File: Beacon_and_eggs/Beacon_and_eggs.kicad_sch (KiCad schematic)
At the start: 40 parts, among them J1 USB_C_Receptacle_USB2.0_16P, Q1 IRLML0030, SW1 Boot, SW2 Reset, U1 SA818V, U2 STM32F411CEUx, U3 ADXL343, U6 MCP1253-33X50I/MS, U7 MCP1253-33X50I/MS, Y1 25MHz 18pF, Y2 32.768kHz 12.5pF

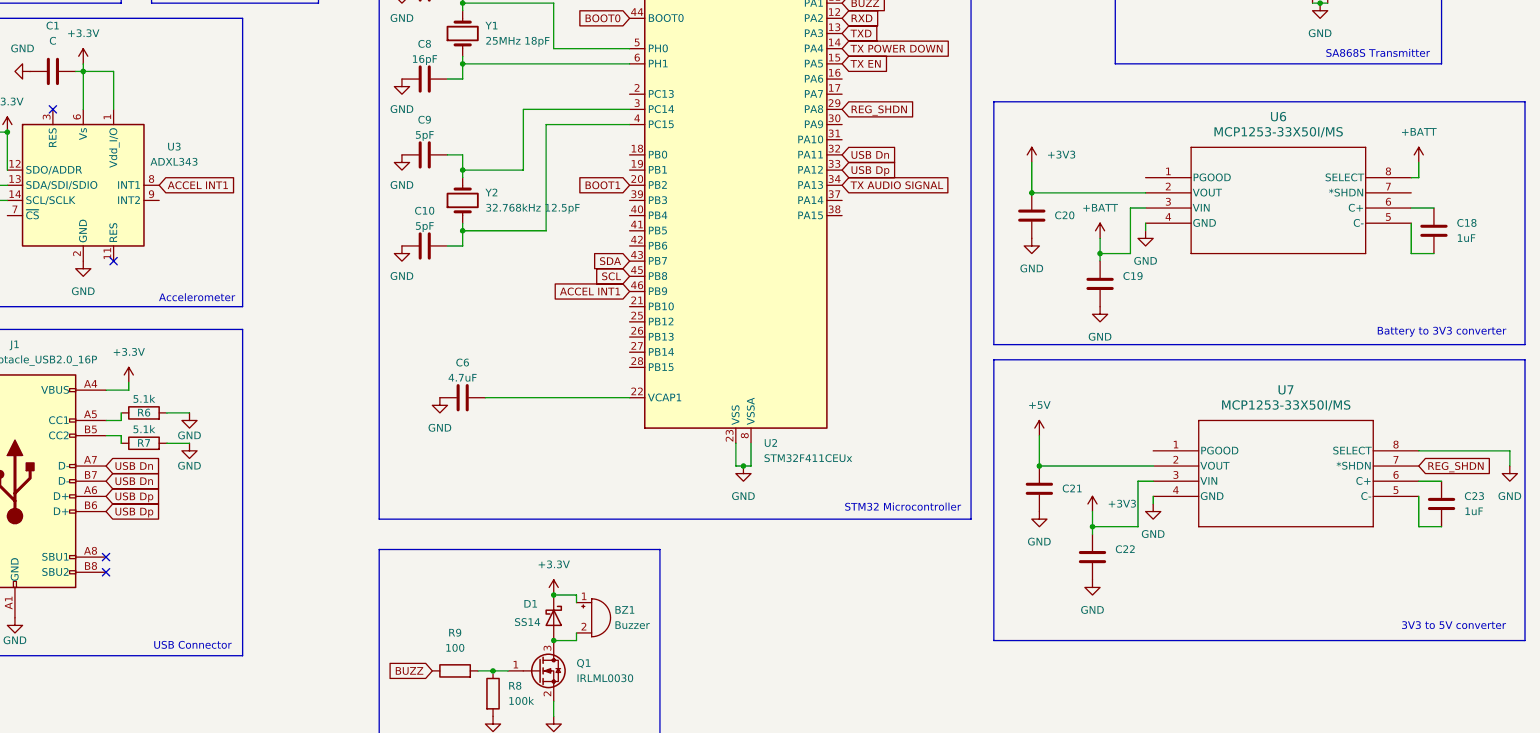
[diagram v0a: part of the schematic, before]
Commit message: Laid traces and changed 3.3V regulator
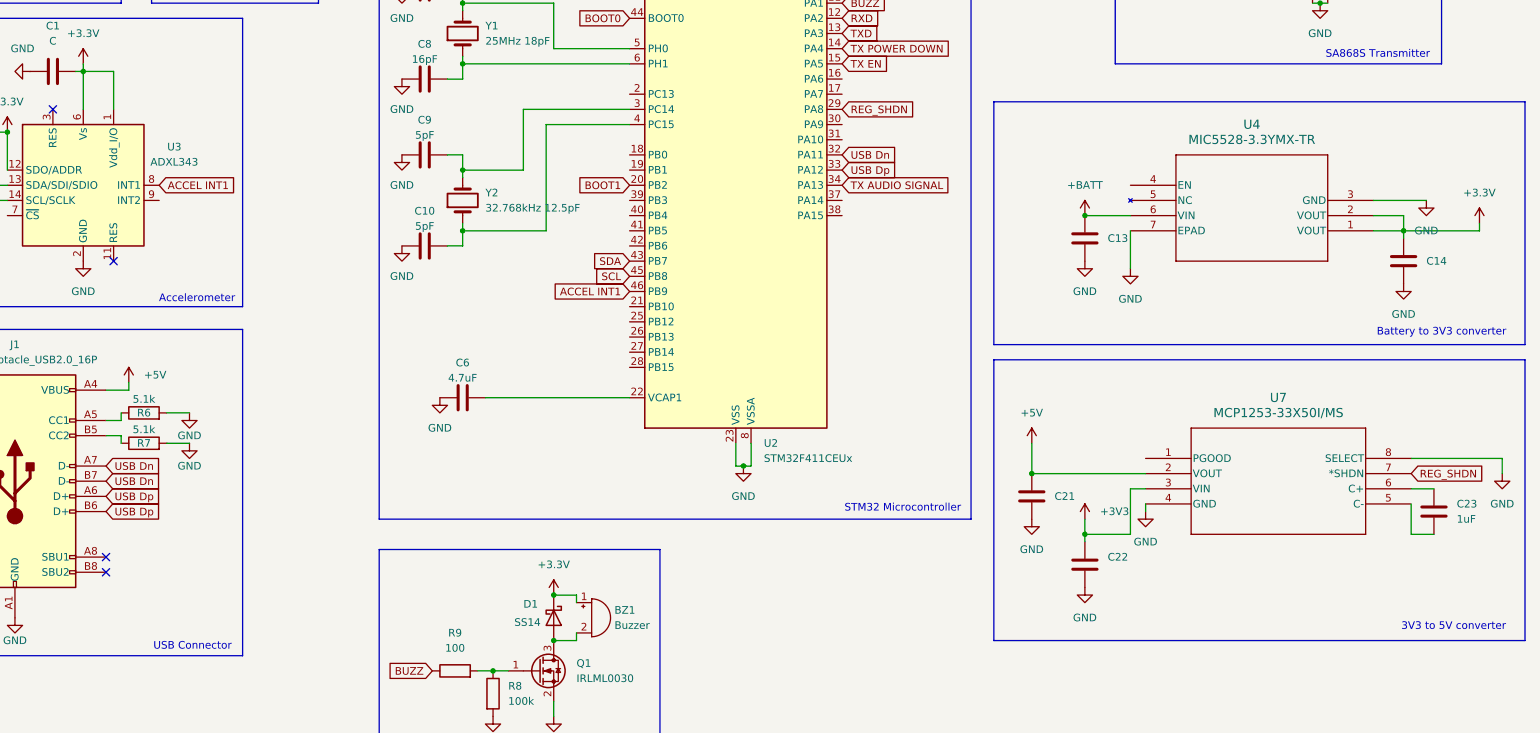
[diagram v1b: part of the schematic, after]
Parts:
- removed C18: 1uF, Capacitor_SMD:C_0603_1608Metric, symbol Device:C
- removed C19: 10uF, Capacitor_SMD:C_0603_1608Metric, symbol Device:C
- removed U6: MCP1253-33X50I/MS, Package_DFN_QFN:TDFN-8-1EP_3x2mm_P0.5mm_EP1.3x1.4mm, symbol 2025_26-UVR-Beacon:MCP1253-33X50I_MS
- added C14: 2.2uF, Capacitor_SMD:C_0603_1608Metric, symbol Device:C
- added U4: MIC5528-3.3YMX-TR, XTDFN6_1P2X1P2_MCH, symbol 2026-01-16_07-07-07:MIC5528-3.3YMX-TR
- C13: renamed from C20; value 10uF -> 2.2uF
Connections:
- net +3.3V: now also C14.1, U4.1 (VOUT), U4.2 (VOUT); no longer J1.A4 (VBUS), J1.A9 (VBUS), J1.B4 (VBUS), J1.B9 (VBUS)
- net +3V3: no longer C13.1
- net +5V: now also J1.A4 (VBUS), J1.A9 (VBUS), J1.B4 (VBUS), J1.B9 (VBUS)
- net +BATT: now also C13.1, U4.6 (VIN)
- net GND: now also C14.2, U4.3 (GND), U4.7 (EPAD)
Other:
- moved on the sheet: C13, C21, C22, C23, U7

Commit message: cheanged schematic and V1 pcb layout completed.
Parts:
- removed BZ1: Buzzer, symbol Device:Buzzer
- removed D1: SS14, Diode_SMD:D_SMA, symbol Diode:SS14
- removed Q1: IRLML0030, Package_TO_SOT_SMD:SOT-23, symbol Transistor_FET:IRLML0030
- removed SW1: Boot, symbol Switch:SW_MEC_5E
- removed SW2: Reset, symbol Switch:SW_MEC_5E
- removed U7: MCP1253-33X50I/MS, Package_DFN_QFN:TDFN-8-1EP_3x2mm_P0.5mm_EP1.3x1.4mm, symbol 2025_26-UVR-Beacon:MCP1253-33X50I_MS
- added 3V3: 3V3, TestPoint:TestPoint_THTPad_D1.5mm_Drill0.7mm, symbol Connector:TestPoint
- added C15: 10uF, Capacitor_SMD:C_0402_1005Metric_Pad0.74x0.62mm_HandSolder, symbol Device:C
- added C16, C18, C20: 0.1uF, Capacitor_SMD:C_0402_1005Metric_Pad0.74x0.62mm_HandSolder, symbol Device:C
- added C17: 1nF, Capacitor_SMD:C_0402_1005Metric_Pad0.74x0.62mm_HandSolder, symbol Device:C_Small
- added C19: 33uF, Capacitor_SMD:C_0402_1005Metric_Pad0.74x0.62mm_HandSolder, symbol Device:C
- added C24: 10nF, Capacitor_SMD:C_0402_1005Metric_Pad0.74x0.62mm_HandSolder, symbol Device:C
- added C25: 33nF, Capacitor_SMD:C_0402_1005Metric_Pad0.74x0.62mm_HandSolder, symbol Device:C
- added D1, D3: UCLAMP3311P.TCT, Diode_SMD:D_0402_1005Metric_Pad0.77x0.64mm_HandSolder, symbol APV2:UCLAMP3311P.TCT
- added D2: RED LED, LED_SMD:LED_0402_1005Metric_Pad0.77x0.64mm_HandSolder, symbol Device:LED
- added D4: BLUE LED, LED_SMD:LED_0402_1005Metric_Pad0.77x0.64mm_HandSolder, symbol Device:LED
- added D5: GREEN LED, LED_SMD:LED_0402_1005Metric_Pad0.77x0.64mm_HandSolder, symbol Device:LED
- added J2: Conn_01x03_Pin, Connector_PinHeader_2.54mm:PinHeader_1x03_P2.54mm_Vertical, symbol Connector:Conn_01x03_Pin
- added J3: Conn_01x02_Pin, Connector_JST:JST_PH_B2B-PH-K_1x02_P2.00mm_Vertical, symbol Connector:Conn_01x02_Pin
- added Q1: NTA4151P, NTA4151PT1G:SOT50P160X90-3N, symbol APV2:NTA4151P
- added Q2: NTA4153N, NTA4151PT1G:SOT50P160X90-3N, symbol APV2:NTA4153N
- added R10, R11, R18: 51k, Resistor_SMD:R_0402_1005Metric_Pad0.72x0.64mm_HandSolder, symbol Device:R
- added R12: 250R, Resistor_SMD:R_0402_1005Metric_Pad0.72x0.64mm_HandSolder, symbol Device:R
- added R13: 37.4K, Resistor_SMD:R_0402_1005Metric_Pad0.72x0.64mm_HandSolder, symbol Device:R
- added R14, R15: 1.5K, Resistor_SMD:R_0402_1005Metric_Pad0.72x0.64mm_HandSolder, symbol Device:R
- added R16: 510k, Resistor_SMD:R_0402_1005Metric_Pad0.72x0.64mm_HandSolder, symbol Device:R
- added R17: 50R, Resistor_SMD:R_0402_1005Metric_Pad0.72x0.64mm_HandSolder, symbol Device:R
- added R19: 3.3K, Resistor_SMD:R_0402_1005Metric_Pad0.72x0.64mm_HandSolder, symbol Device:R
- added R20: 1K, Resistor_SMD:R_0402_1005Metric_Pad0.72x0.64mm_HandSolder, symbol Device:R
- added SIG: FABRIC_ANT_HOLES, MountingHole:MountingHole_3.2mm_M3_DIN965_Pad_TopBottom, symbol Connector:Conn_01x02_Pin
- added SW3: RESET, Button_Switch_SMD:SW_SPST_PTS810, symbol Switch:SW_MEC_5G
- added SW4: BOOT0, Button_Switch_SMD:SW_SPST_PTS810, symbol Switch:SW_MEC_5G
- added TP3: SCL, TestPoint:TestPoint_THTPad_D1.5mm_Drill0.7mm, symbol Connector:TestPoint
- added TP4: SDA, TestPoint:TestPoint_THTPad_D1.5mm_Drill0.7mm, symbol Connector:TestPoint
- added TP5: VBAT, TestPoint:TestPoint_THTPad_D1.5mm_Drill0.7mm, symbol Connector:TestPoint
- added TP6: VSYS, TestPoint:TestPoint_THTPad_D1.5mm_Drill0.7mm, symbol Connector:TestPoint
- added U6: BQ24070RHLR, Package_SO:HTSSOP-20-1EP_4.4x6.5mm_P0.65mm_EP3.4x6.5mm_Mask2.4x3.7mm, symbol BQ24070RHLR:BQ24070RHLR
- C1: value C -> 0.1F; footprint Capacitor_SMD:C_0603_1608Metric -> Capacitor_SMD:C_0402_1005Metric_Pad0.74x0.62mm_HandSolder
- C10, C7, C8, C9: footprint Capacitor_SMD:C_0201_0603Metric -> Capacitor_SMD:C_0402_1005Metric_Pad0.74x0.62mm_HandSolder
- C11, C12, C13, C14, C21: footprint Capacitor_SMD:C_0603_1608Metric -> Capacitor_SMD:C_0402_1005Metric_Pad0.74x0.62mm_HandSolder
- C2, C3, C6: footprint Capacitor_SMD:C_0201_0603Metric -> Capacitor_SMD:C_0201_0603Metric_Pad0.64x0.40mm_HandSolder
- C22: value 10uF -> 0.1uF; footprint Capacitor_SMD:C_0603_1608Metric -> Capacitor_SMD:C_0402_1005Metric_Pad0.74x0.62mm_HandSolder
- C23: value 1uF -> 10uF; footprint Capacitor_SMD:C_0603_1608Metric -> Capacitor_SMD:C_0402_1005Metric_Pad0.74x0.62mm_HandSolder
- C4, C5: footprint Capacitor_SMD:C_0603_1608Metric -> Capacitor_SMD:C_0201_0603Metric_Pad0.64x0.40mm_HandSolder
- J1: footprint (none) -> Connector_USB:USB_C_Receptacle_GCT_USB4105-xx-A_16P_TopMnt_Horizontal
- R1, R2, R3, R4, R5, R6, R7: footprint Resistor_SMD:R_0603_1608Metric -> Resistor_SMD:R_0402_1005Metric_Pad0.72x0.64mm_HandSolder
- R8: value 100k -> 250R; footprint Resistor_SMD:R_0603_1608Metric -> Resistor_SMD:R_0402_1005Metric_Pad0.72x0.64mm_HandSolder
- R9: value 100 -> 250R; footprint Resistor_SMD:R_0603_1608Metric -> Resistor_SMD:R_0402_1005Metric_Pad0.72x0.64mm_HandSolder
- U4: footprint XTDFN6_1P2X1P2_MCH -> footprints:XTDFN6_1P2X1P2_MCH
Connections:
- net +3V3 is gone; now on net VBUS: C22.1
- net +BATT is gone; now on net VSYS: C13.1, U4.6 (VIN)
- net +3.3V: now also 3V3.1, R17.1, SW4.3 (B), SW4.4 (B); no longer C1.2, U1.8 (VDD), U3.1 (Vdd_I/O)
- net BOOT0: now also R1.2, SW4.1 (A), SW4.2 (A); no longer R1.1
- net GND: now also C1.2, C23.2, R1.1, C15.2, C16.2, C17.2, C18.2, C19.2, C20.2, C24.2, C25.2, D1.1 (A1), D3.1 (A1), D4.1 (K), J2.3 (Pin_3), J3.2 (Pin_2), Q2.2 (S), R13.2, R16.2, R18.1, R20.2, SIG.2 (Pin_2), SW3.3 (B), SW3.4 (B), U6.11 (VSS_11), U6.19 (GND_19), U6.20 (GND_20), U6.21 (VSS_21), U6.22 (VSS_21), U6.23 (VSS_21), U6.24 (VSS_21), U6.25 (VSS_21), U6.26 (VSS_21), U6.27 (VSS_21), U6.28 (VSS_21), U6.29 (VSS_21), U6.8 (MODE); no longer C1.1, R1.2, R8.2
- net NRST: now also SW3.1 (A), SW3.2 (A)
- net SCL: now also R4.1, TP3.1; no longer R5.1
- net SDA: now also R5.1, TP4.1; no longer R4.1
- net X2_OUT: now reaches C10.2, U2.4 (PC15), Y2.1
- net X2_IN: now reaches C9.2, U2.3 (PC14), Y2.2
- net VBUS: now reaches C23.1
- net VBUS: now also J1.A4 (VBUS), J1.A9 (VBUS), J1.B4 (VBUS), J1.B9 (VBUS), U6.4 (IN)
- net LED1: now reaches U2.17 (PA7)
- net LED1: now also R12.1
- net TX_AUDIO_SIGNAL: now reaches U2.31 (PA10)
- net TX_AUDIO_SIGNAL: now also R19.1
- net SWCLK: now reaches U2.37 (PA14)
- net SWCLK: now also R9.1, J2.1 (Pin_1)
- net BATT_V_ADC: now reaches U2.38 (PA15)
- net BATT_V_ADC: now also C17.1, R11.1, R18.2
- net BATT_EN: now reaches U2.41 (PB5)
- net BATT_EN: now also Q2.1 (G), R16.1
- net X1_IN: now reaches C7.2, U2.5 (PH0), Y1.2
- net X1_OUT: now reaches C8.2, U2.6 (PH1), Y1.1
- net at R9.2: now also D3.2 (A2); no longer R8.1
- net VSYS: now reaches U4.4 (EN)
- net VSYS: now also C21.1, U1.8 (VDD), C16.1, C20.1, TP6.1, U6.15 (OUT_15), U6.16 (OUT_16), U6.17 (OUT_17)
- removed net +5V: C21.1, J1.A4 (VBUS), J1.A9 (VBUS), J1.B4 (VBUS), J1.B9 (VBUS)
- net ACCEL INT1 renamed ACCEL_INT1
- net BUZZ: no longer names the net of U2.11 (PA1)
- net BUZZ: no longer R9.1
- net REG_SHDN: no longer names the net of U2.29 (PA8)
- net RF_IN renamed ANT_SIG
- net ANT_SIG: now also SIG.1 (Pin_1)
- net TX AUDIO SIGNAL: no longer names the net of U1.18 (MIC_IN)
- net TX AUDIO SIGNAL: now also C25.1, R19.2; no longer U2.34 (PA13)
- net TX EN renamed TX_EN
- net TX POWER DOWN renamed TX_PWR_DN
- net USB Dn renamed USB_DN
- net USB Dp renamed USB_DP
- new net: Q1.3 (D1), Q1.8 (D1), R11.2
- new net: R20.1, U6.10 (ISET1)
- new net: C24.1, R13.1, U6.13 (DPPM)
- new net: D2.1 (K), U6.2 (STAT1)
- new net: D5.1 (K), U6.3 (STAT2)
- new net: C15.1, R17.2
- new net: D4.2 (A), R12.2
- new net: C1.1, U3.1 (Vdd_I/O)
- new net: D5.2 (A), R14.2
- new net: D2.2 (A), R15.2
- new net: D1.2 (A2), R8.1
- new net: Q1.1 (G1), Q2.3 (D), R10.1
- new net SWDIO: J2.2 (Pin_2), R8.2, U2.34 (PA13)
- new net VBAT: C19.1, J3.1 (Pin_1), Q1.2 (S1), R10.2, TP5.1, U6.5 (BAT_5), U6.6 (BAT_6)
- new net VREF: C18.1, R14.1, R15.1, U6.1 (VREF), U6.14 (TMR), U6.7 (ISET2), U6.9 (CE)
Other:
- note added: "ACCEELEROMETER"
- note added: "ANTENNA INPUT"
- note added: "BATTERY CHARGER AND FLOW CONTROL"
- note added: "BATTERY CONNECTOR"
- note added: "BATTERY MONITORING CIRCUIT"
- note added: "BOOT CIRCUIT"
- note added: "MICROCONTROLLER"
- note added: "Pads are plated mounting holes used as RF feed and GND clamp for fabric antenna. No connector installed"
- note added: "RESET CIRCUIT"
- note added: "SA868S TRANSMITTER"
- note added: "SWD CONNECTOR"
- note added: "TEST POINTS"
- note added: "USB-C CONNECTOR"
- note added: "VSYS TO 3V3 REG"
- note removed: "3V3 to 5V converter"
- note removed: "Accelerometer"
- note removed: "Battery to 3V3 converter"
- note removed: "Boot circuit"
- note removed: "Buzzer"
- note removed: "Reset circuit"
- note removed: "SA868S Transmitter"
- note removed: "STM32 Microcontroller"
- note removed: "USB Connector"
- moved on the sheet: C10, C11, C12, C2, C3, C4, C5, C6, C7, C8, C9, J1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

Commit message: narrowed the pcb down from 60mm to 40 mm
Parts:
- renumbered SIG to SIG1
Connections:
- net ACCEL_INT1: now also U2.2 (PC13); no longer U2.46 (PB9)
- net BATT_EN: now also U2.28 (PB15); no longer U2.41 (PB5)
- net BATT_V_ADC: now also U2.16 (PA6); no longer U2.38 (PA15)
- net LED1: now also U2.13 (PA3); no longer U2.17 (PA7)
- net RXD: now also U2.18 (PB0); no longer U2.12 (PA2)
- net TXD: now also U2.25 (PB12); no longer U2.13 (PA3)
- net TX_AUDIO_SIGNAL: now also U2.26 (PB13); no longer U2.31 (PA10)
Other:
- moved on the sheet: C10, C7, C8, C9, Y1, Y2

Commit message: Added complete BOM, replaced a footprint, added missing STEP files
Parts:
- 3V3: Manufacturer (none) -> C0402C104K4RACTU; now left out of the parts list
- C1: value 0.1F -> 0.1uF; DigiKey_Part_Number (none) -> C0402C104K4RACTU
- C10, C9: DigiKey_Part_Number (none) -> GRM1555C1H5R0BA01D
- C11, C12: value 0.1uf -> 0.1uF; DigiKey_Part_Number (none) -> C0402C104K4RACTU
- C13, C14: DigiKey_Part_Number (none) -> GRM155C80J225KE95D
- C15, C21, C23: DigiKey_Part_Number (none) -> GRM155R61A106ME11D
- C16, C18, C20, C22: DigiKey_Part_Number (none) -> C0402C104K4RACTU
- C17: DigiKey_Part_Number (none) -> C0402C102K5RACTU; Manufacturer Part Number 0201B102K250CT -> (none)
- C19: footprint Capacitor_SMD:C_0402_1005Metric_Pad0.74x0.62mm_HandSolder -> Capacitor_SMD:C_0805_2012Metric; DigiKey_Part_Number (none) -> C2012X5R0J336M125AC
- C2, C3, C4, C5: DigiKey_Part_Number (none) -> GRM033C71C104KE14D
- C24: DigiKey_Part_Number (none) -> GRM155R71C103KA01D
- C25: DigiKey_Part_Number (none) -> C0402C333J4RACTU
- C6: DigiKey_Part_Number (none) -> GRM155R60J475ME87D
- C7, C8: DigiKey_Part_Number (none) -> GJM1555C1H160FB01J
- D1, D3: DigiKey_Part_Number (none) -> UCLAMP3311P.TCT
- D2: DigiKey_Part_Number (none) -> SML-D12U1WT86
- D4: footprint LED_SMD:LED_0402_1005Metric_Pad0.77x0.64mm_HandSolder -> LED_SMD:LED_0805_2012Metric; DigiKey_Part_Number (none) -> 150080BS75000; Manufacturer Part Number 150080BS75000 -> (none)
- D5: DigiKey_Part_Number (none) -> 150060GS75000
- J1: DigiKey_Part_Number (none) -> USB4215-03-A
- J2, J3, SIG1, TP3, TP4, TP5, TP6: now left out of the parts list
- Q1: DigiKey_Part_Number (none) -> NTA4151PT1G
- Q2: DigiKey_Part_Number (none) -> NTA4153NT1G
- R1, R2, R3: DigiKey_Part_Number (none) -> RMCF0402FT10K0
- R10, R11, R18: DigiKey_Part_Number (none) -> ERA-2AEB513X; Manufacturer Part Number RC0201FR-0751KL -> (none)
- R12: DigiKey_Part_Number (none) -> RE0402BRE07250RL; Manufacturer Part Number RMCF0603FT22R0 -> (none)
- R13: DigiKey_Part_Number (none) -> ERJ-2RKF3742X
- R14, R15: DigiKey_Part_Number (none) -> RC0402FR-071K5L
- R16: DigiKey_Part_Number (none) -> RC0402FR-07510KL; Manufacturer Part Number RC0201FR-07510KL -> (none)
- R17: DigiKey_Part_Number (none) -> RT0402BRE0750RL
- R19: DigiKey_Part_Number (none) -> ERA-2AEB332X
- R20: DigiKey_Part_Number (none) -> RC0402FR-071KL
- R4, R5: DigiKey_Part_Number (none) -> RC0402JR-074K7L
- R6, R7: DigiKey_Part_Number (none) -> RC0402FR-075K1L
- R8, R9: DigiKey_Part_Number (none) -> RE0402BRE07250RL
- SW3, SW4: DigiKey_Part_Number (none) -> PTS810SJK250SMTR LFS
- U1: value SA818V -> SA868S; DigiKey_Part_Number (none) -> SA868S
- U2: value STM32F411CEUx -> STM32F411CEU6TR; DigiKey_Part_Number (none) -> STM32F411CEU6TR
- U3: DigiKey_Part_Number (none) -> ADXL343BCCZ-RL7
- U4: DigiKey_Part_Number (none) -> MIC5528-3.3YMX-TR
- U6: footprint Package_SO:HTSSOP-20-1EP_4.4x6.5mm_P0.65mm_EP3.4x6.5mm_Mask2.4x3.7mm -> BQ24070RHLR:RHL20_2P05X3P05; symbol BQ24070RHLR:BQ24070RHLR -> 2026-04-28_05-53-34:BQ24070RHLR
- Y1: DigiKey_Part_Number (none) -> ABM3-25.000MHZ-D2Y-T
- Y2: DigiKey_Part_Number (none) -> 12.87167
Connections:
- net GND: no longer U6.21 (VSS_21), U6.22 (VSS_21), U6.23 (VSS_21), U6.24 (VSS_21), U6.25 (VSS_21), U6.26 (VSS_21), U6.27 (VSS_21), U6.28 (VSS_21), U6.29 (VSS_21), U6.8 (MODE)
- net VREF: no longer U6.7 (ISET2)
- no-connect marks 6 -> 13
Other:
- moved on the sheet: C13, C14, C17, C18, C19, C20, C21, C22, C23, C24, D2, D4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
